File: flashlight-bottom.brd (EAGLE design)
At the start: 33 x 33 mm, 1 part, among them SW1 DIL3-TOGGLE-SWITCHDIL3

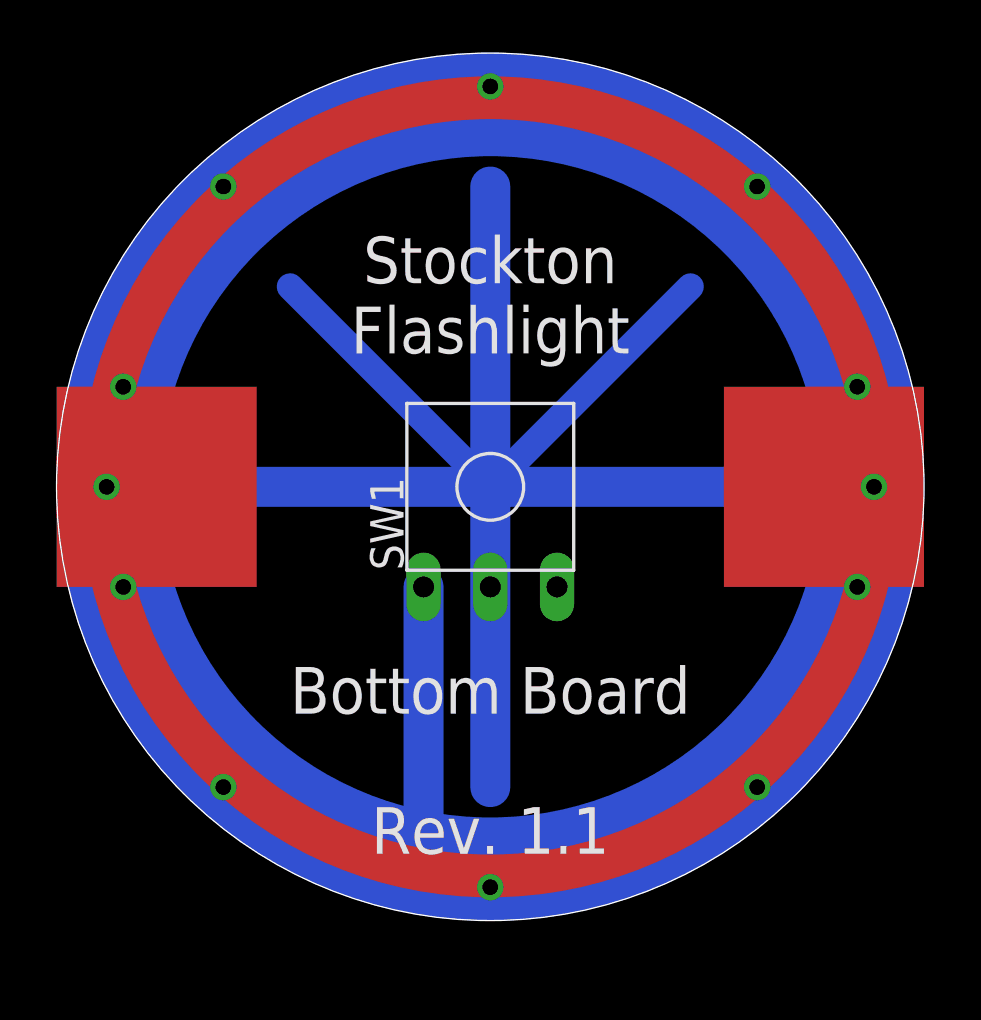
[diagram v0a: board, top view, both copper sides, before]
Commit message: rev 2.0 of the bottom board, plus minor tweaks to the top board
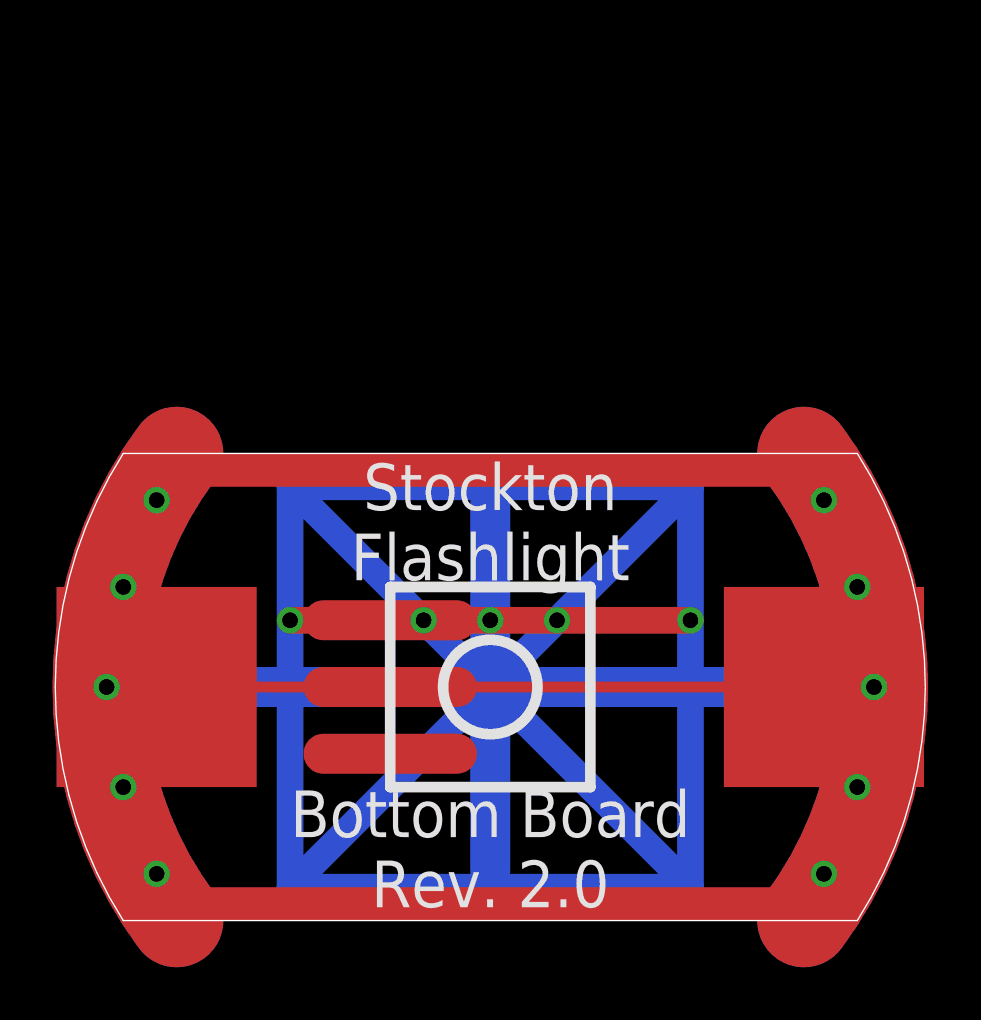
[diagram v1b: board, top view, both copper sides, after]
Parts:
- removed SW1: DIL3-TOGGLE-SWITCHDIL3, chrisy-components:DIL3-TOGGLE-SWITCH
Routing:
- net N$2: track 44.4 -> 156.1 mm, vias 0 -> 5
- net N$16: track 0.00 -> 35.6 mm
- net N$10: track 0.00 -> 33.0 mm, vias 1 -> 0
- net N$5: track 8.89 -> 35.6 mm
- net N$3: track 22.9 -> 0.00 mm
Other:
- board size 33 x 33 mm -> 33.1 x 17.8 mm
- board text added: "Bottom Board Rev. 2.0"
- board text removed: "Bottom Board Rev. 1.1"
- board text removed: "Rev. 1.1"
- board text removed: "SPRING"
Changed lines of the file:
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@@
 <board>
 <plain>
-<circle x="16.51" y="16.51" radius="16.51" width="0.040640625" layer="20"/>
-<circle x="16.51" y="16.51" radius="14.5542" width="3.937" layer="16"/>
-<text x="16.51" y="21.59" size="1.778" layer="25" align="bottom-center">Stockton
+<text x="16.51" y="12.954" size="1.778" layer="25" align="bottom-center">Stockton
 Flashlight</text>
-<circle x="16.51" y="16.51" radius="14.7574" width="3.556" layer="30"/>
-<text x="16.51" y="2.54" size="1.778" layer="1" align="bottom-center">Rev. 1.1</text>
-<text x="16.51" y="2.54" size="1.778" layer="25" align="bottom-center">Bottom Board
-Rev. 1.1</text>
-<circle x="16.51" y="16.51" radius="14.810615625" width="1.6256" layer="1"/>
-<wire x1="16.51" y1="16.51" x2="8.89" y2="24.13" width="1.016" layer="30"/>
-<wire x1="16.51" y1="16.51" x2="5.08" y2="16.51" width="1.524" layer="30"/>
-<wire x1="16.51" y1="16.51" x2="27.94" y2="16.51" width="1.524" layer="30"/>
-<wire x1="16.51" y1="16.51" x2="24.13" y2="24.13" width="1.016" layer="30"/>
-<wire x1="16.51" y1="16.51" x2="16.51" y2="27.94" width="1.524" layer="30"/>
-<wire x1="16.51" y1="16.51" x2="16.51" y2="15.24" width="1.524" layer="30"/>
-<wire x1="16.51" y1="10.16" x2="16.51" y2="5.08" width="1.524" layer="30"/>
-<circle x="16.51" y="16.51" radius="6.35" width="0.4064" layer="22"/>
-<text x="22.352" y="14.605" size="1.016" layer="26" rot="MR0">SPRING</text>
-<rectangle x1="25.4" y1="12.7" x2="33.02" y2="20.32" layer="1"/>
-<rectangle x1="25.4" y1="12.7" x2="33.02" y2="20.32" layer="29"/>
-<rectangle x1="0" y1="12.7" x2="7.62" y2="20.32" layer="29"/>
-<rectangle x1="0" y1="12.7" x2="7.62" y2="20.32" layer="1"/>
+<text x="16.51" y="0.508" size="1.778" layer="25" align="bottom-center">Bottom Board
+Rev. 2.0</text>
+<wire x1="16.51" y1="8.89" x2="8.89" y2="16.51" width="1.016" layer="30"/>
+<wire x1="16.51" y1="8.89" x2="5.08" y2="8.89" width="1.524" layer="30"/>
+<wire x1="16.51" y1="8.89" x2="27.94" y2="8.89" width="1.524" layer="30"/>
+<wire x1="16.51" y1="8.89" x2="24.13" y2="16.51" width="1.016" layer="30"/>
+<wire x1="16.51" y1="8.89" x2="16.51" y2="15.875" width="1.524" layer="30"/>
+<wire x1="16.51" y1="8.89" x2="16.51" y2="1.905" width="1.524" layer="30"/>
+<circle x="16.51" y="8.89" radius="6.35" width="0.4064" layer="22"/>
+<rectangle x1="25.4" y1="5.08" x2="33.02" y2="12.7" layer="1"/>
+<rectangle x1="25.4" y1="5.08" x2="33.02" y2="12.7" layer="29"/>
+<rectangle x1="0" y1="5.08" x2="7.62" y2="12.7" layer="29"/>
+<rectangle x1="0" y1="5.08" x2="7.62" y2="12.7" layer="1"/>
+<wire x1="2.54" y1="17.78" x2="2.54" y2="0" width="0.0508" layer="20" curve="64.94"/>
+<wire x1="30.48" y1="0" x2="30.48" y2="17.78" width="0.0508" layer="20" curve="64.94"/>
+<wire x1="2.54" y1="0" x2="30.48" y2="0" width="0.0508" layer="20"/>
+<wire x1="30.48" y1="17.78" x2="2.54" y2="17.78" width="0.0508" layer="20"/>
+<wire x1="4.572" y1="17.78" x2="4.572" y2="0" width="3.556" layer="30" curve="73.34" cap="flat"/>
+<wire x1="28.448" y1="0" x2="28.448" y2="17.78" width="3.556" layer="30" curve="73.34" cap="flat"/>
+<rectangle x1="2.54" y1="0" x2="30.48" y2="1.27" layer="1"/>
+<rectangle x1="2.54" y1="16.51" x2="30.48" y2="17.78" layer="1"/>
+<wire x1="16.51" y1="8.89" x2="8.89" y2="1.27" width="1.016" layer="30"/>
+<wire x1="16.51" y1="8.89" x2="24.13" y2="1.27" width="1.016" layer="30"/>
+<wire x1="10.16" y1="8.89" x2="15.24" y2="8.89" width="1.524" layer="29"/>
+<wire x1="10.16" y1="11.43" x2="15.24" y2="11.43" width="1.524" layer="29"/>
+<wire x1="10.16" y1="6.35" x2="15.24" y2="6.35" width="1.524" layer="29"/>
+<wire x1="12.7" y1="12.7" x2="20.32" y2="12.7" width="0.4064" layer="25"/>
+<wire x1="20.32" y1="12.7" x2="20.32" y2="5.08" width="0.4064" layer="25"/>
+<wire x1="20.32" y1="5.08" x2="12.7" y2="5.08" width="0.4064" layer="25"/>
+<wire x1="12.7" y1="5.08" x2="12.7" y2="12.7" width="0.4064" layer="25"/>
+<circle x="16.51" y="8.89" radius="1.79605" width="0.4064" layer="25"/>
 </plain>
 <attributes>
@@
 </autorouter>
 <elements>
-<element name="SW1" library="chrisy-components" package="DIL3-TOGGLE-SWITCH" value="DIL3-TOGGLE-SWITCHDIL3" x="16.51" y="16.51"/>
 </elements>
 <signals>
 <signal name="N$1">
-<via x="1.905" y="16.51" extent="1-16" drill="0.6"/>
+<via x="1.905" y="8.89" extent="1-16" drill="0.6"/>
 </signal>
 <signal name="N$4">
-<via x="31.115" y="16.51" extent="1-16" drill="0.6"/>
+<via x="31.115" y="8.89" extent="1-16" drill="0.6"/>
 </signal>
 <signal name="N$2">
-<wire x1="5.08" y1="16.51" x2="16.51" y2="16.51" width="1.524" layer="16"/>
-<wire x1="16.51" y1="16.51" x2="27.94" y2="16.51" width="1.524" layer="16"/>
-<wire x1="16.51" y1="16.51" x2="8.89" y2="24.13" width="1.016" layer="16"/>
-<wire x1="16.51" y1="16.51" x2="24.13" y2="24.13" width="1.016" layer="16"/>
-</signal>
-<signal name="N$3">
-<wire x1="16.51" y1="27.94" x2="16.51" y2="5.08" width="1.524" layer="16"/>
+<wire x1="5.08" y1="8.89" x2="16.51" y2="8.89" width="1.524" layer="16"/>
+<wire x1="16.51" y1="8.89" x2="27.94" y2="8.89" width="1.524" layer="16"/>
+<wire x1="16.51" y1="8.89" x2="13.97" y2="11.43" width="1.016" layer="16"/>
+<wire x1="13.97" y1="11.43" x2="8.89" y2="16.51" width="1.016" layer="16"/>
+<wire x1="16.51" y1="8.89" x2="19.05" y2="11.43" width="1.016" layer="16"/>
+<wire x1="19.05" y1="11.43" x2="24.13" y2="16.51" width="1.016" layer="16"/>
+<wire x1="16.51" y1="8.89" x2="8.89" y2="1.27" width="1.016" layer="16"/>
+<wire x1="16.51" y1="8.89" x2="24.13" y2="1.27" width="1.016" layer="16"/>
+<wire x1="24.13" y1="1.27" x2="8.89" y2="1.27" width="1.016" layer="16"/>
+<wire x1="8.89" y1="1.27" x2="8.89" y2="11.43" width="1.016" layer="16"/>
+<wire x1="8.89" y1="11.43" x2="8.89" y2="16.51" width="1.016" layer="16"/>
+<wire x1="8.89" y1="16.51" x2="24.13" y2="16.51" width="1.016" layer="16"/>
+<wire x1="24.13" y1="16.51" x2="24.13" y2="11.43" width="1.016" layer="16"/>
+<wire x1="24.13" y1="11.43" x2="24.13" y2="1.27" width="1.016" layer="16"/>
+<wire x1="8.89" y1="11.43" x2="13.97" y2="11.43" width="1.016" layer="1"/>
+<via x="8.89" y="11.43" extent="1-16" drill="0.6"/>
+<wire x1="13.97" y1="11.43" x2="16.51" y2="11.43" width="1.016" layer="1"/>
+<wire x1="16.51" y1="11.43" x2="19.05" y2="11.43" width="1.016" layer="1"/>
+<wire x1="19.05" y1="11.43" x2="24.13" y2="11.43" width="1.016" layer="1"/>
+<wire x1="16.51" y1="15.875" x2="16.51" y2="11.43" width="1.524" layer="16"/>
+<wire x1="16.51" y1="11.43" x2="16.51" y2="1.905" width="1.524" layer="16"/>
+<via x="16.51" y="11.43" extent="1-16" drill="0.6"/>
+<via x="24.13" y="11.43" extent="1-16" drill="0.6"/>
+<via x="19.05" y="11.43" extent="1-16" drill="0.6"/>
+<via x="13.97" y="11.43" extent="1-16" drill="0.6"/>
+</signal>
+<signal name="N$12">
+<via x="2.54" y="12.7" extent="1-16" drill="0.6"/>
+</signal>
+<signal name="N$13">
+<via x="2.54" y="5.08" extent="1-16" drill="0.6"/>
+</signal>
+<signal name="N$14">
+<via x="30.48" y="5.08" extent="1-16" drill="0.6"/>
+</signal>
+<signal name="N$15">
+<via x="30.48" y="12.7" extent="1-16" drill="0.6"/>
+</signal>
+<signal name="N$16">
+<wire x1="4.572" y1="17.78" x2="4.572" y2="0" width="3.556" layer="16" curve="73.34" cap="flat"/>
+<wire x1="28.448" y1="0" x2="28.448" y2="17.78" width="3.556" layer="16" curve="73.34" cap="flat"/>
 </signal>
 <signal name="N$5">
-<wire x1="13.97" y1="3.81" x2="13.97" y2="12.7" width="1.524" layer="16"/>
+<wire x1="4.572" y1="17.78" x2="4.572" y2="0" width="3.556" layer="1" curve="73.34" cap="flat"/>
+<wire x1="28.448" y1="0" x2="28.448" y2="17.78" width="3.556" layer="1" curve="73.34" cap="flat"/>
 </signal>
 <signal name="N$6">
-<via x="16.51" y="1.27" extent="1-16" drill="0.6"/>
+<via x="3.81" y="1.778" extent="1-16" drill="0.6"/>
 </signal>
 <signal name="N$7">
-<via x="16.51" y="31.75" extent="1-16" drill="0.6"/>
+<via x="3.81" y="16.002" extent="1-16" drill="0.6"/>
 </signal>
 <signal name="N$8">
-<via x="6.35" y="27.94" extent="1-16" drill="0.6"/>
+<via x="29.21" y="1.778" extent="1-16" drill="0.6"/>
 </signal>
 <signal name="N$9">
-<via x="26.67" y="27.94" extent="1-16" drill="0.6"/>
+<via x="29.21" y="16.002" extent="1-16" drill="0.6"/>
 </signal>
 <signal name="N$10">
-<via x="26.67" y="5.08" extent="1-16" drill="0.6"/>
-</signal>
-<signal name="N$11">
-<via x="6.35" y="5.08" extent="1-16" drill="0.6"/>
-</signal>
-<signal name="N$12">
-<via x="2.54" y="20.32" extent="1-16" drill="0.6"/>
-</signal>
-<signal name="N$13">
-<via x="2.54" y="12.7" extent="1-16" drill="0.6"/>
-</signal>
-<signal name="N$14">
-<via x="30.48" y="12.7" extent="1-16" drill="0.6"/>
-</signal>
-<signal name="N$15">
-<via x="30.48" y="20.32" extent="1-16" drill="0.6"/>
+<wire x1="5.08" y1="8.89" x2="10.16" y2="8.89" width="0.4064" layer="1"/>
+<wire x1="15.24" y1="8.89" x2="27.94" y2="8.89" width="0.4064" layer="1"/>
+<wire x1="10.16" y1="8.89" x2="15.24" y2="8.89" width="1.524" layer="1"/>
+<wire x1="10.16" y1="6.35" x2="15.24" y2="6.35" width="1.524" layer="1"/>
+<wire x1="10.16" y1="11.43" x2="15.24" y2="11.43" width="1.524" layer="1"/>
 </signal>
 </signals>

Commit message: rev 3 of the bottom
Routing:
- net N$10: track 33.0 -> 35.6 mm
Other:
- board text added: "3x C battery This end (-)"
- board text added: "Bottom Board Rev. 3.0"
- board text added: "SPRING"
- board text added: "SW1"
- board text removed: "Bottom Board Rev. 2.0"
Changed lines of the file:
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@@
 <board>
 <plain>
-<text x="16.51" y="12.954" size="1.778" layer="25" align="bottom-center">Stockton
+<text x="16.51" y="13.208" size="1.778" layer="29" align="bottom-center">Stockton
 Flashlight</text>
-<text x="16.51" y="0.508" size="1.778" layer="25" align="bottom-center">Bottom Board
-Rev. 2.0</text>
+<text x="16.51" y="0.508" size="1.778" layer="29" align="bottom-center">Bottom Board
+Rev. 3.0</text>
 <wire x1="16.51" y1="8.89" x2="8.89" y2="16.51" width="1.016" layer="30"/>
 <wire x1="16.51" y1="8.89" x2="5.08" y2="8.89" width="1.524" layer="30"/>
@@
 <wire x1="16.51" y1="8.89" x2="16.51" y2="15.875" width="1.524" layer="30"/>
 <wire x1="16.51" y1="8.89" x2="16.51" y2="1.905" width="1.524" layer="30"/>
-<circle x="16.51" y="8.89" radius="6.35" width="0.4064" layer="22"/>
+<circle x="16.51" y="8.89" radius="6.35" width="0.254" layer="22"/>
 <rectangle x1="25.4" y1="5.08" x2="33.02" y2="12.7" layer="1"/>
 <rectangle x1="25.4" y1="5.08" x2="33.02" y2="12.7" layer="29"/>
@@
 <wire x1="16.51" y1="8.89" x2="8.89" y2="1.27" width="1.016" layer="30"/>
 <wire x1="16.51" y1="8.89" x2="24.13" y2="1.27" width="1.016" layer="30"/>
-<wire x1="10.16" y1="8.89" x2="15.24" y2="8.89" width="1.524" layer="29"/>
-<wire x1="10.16" y1="11.43" x2="15.24" y2="11.43" width="1.524" layer="29"/>
-<wire x1="10.16" y1="6.35" x2="15.24" y2="6.35" width="1.524" layer="29"/>
-<wire x1="12.7" y1="12.7" x2="20.32" y2="12.7" width="0.4064" layer="25"/>
-<wire x1="20.32" y1="12.7" x2="20.32" y2="5.08" width="0.4064" layer="25"/>
-<wire x1="20.32" y1="5.08" x2="12.7" y2="5.08" width="0.4064" layer="25"/>
-<wire x1="12.7" y1="5.08" x2="12.7" y2="12.7" width="0.4064" layer="25"/>
-<circle x="16.51" y="8.89" radius="1.79605" width="0.4064" layer="25"/>
+<wire x1="8.89" y1="8.89" x2="15.24" y2="8.89" width="1.524" layer="29"/>
+<wire x1="8.89" y1="11.43" x2="15.24" y2="11.43" width="1.524" layer="29"/>
+<wire x1="8.89" y1="6.35" x2="15.24" y2="6.35" width="1.524" layer="29"/>
+<wire x1="12.7" y1="12.7" x2="20.32" y2="12.7" width="0.254" layer="25"/>
+<wire x1="20.32" y1="12.7" x2="20.32" y2="5.08" width="0.254" layer="25"/>
+<wire x1="20.32" y1="5.08" x2="12.7" y2="5.08" width="0.254" layer="25"/>
+<wire x1="12.7" y1="5.08" x2="12.7" y2="12.7" width="0.254" layer="25"/>
+<circle x="16.51" y="8.89" radius="1.79605" width="0.254" layer="25"/>
+<rectangle x1="7.112" y1="1.27" x2="25.908" y2="5.08" layer="1"/>
+<rectangle x1="7.366" y1="12.7" x2="25.654" y2="16.764" layer="1"/>
+<rectangle x1="7.366" y1="12.446" x2="25.4" y2="12.7" layer="1"/>
+<rectangle x1="7.112" y1="5.08" x2="25.654" y2="5.334" layer="1"/>
+<rectangle x1="3.556" y1="0.762" x2="7.62" y2="5.334" layer="1"/>
+<rectangle x1="25.4" y1="1.016" x2="30.48" y2="5.334" layer="1"/>
+<rectangle x1="25.654" y1="12.7" x2="29.21" y2="16.764" layer="1"/>
+<rectangle x1="3.556" y1="12.446" x2="7.366" y2="16.764" layer="1"/>
+<text x="22.606" y="6.604" size="1.778" layer="25" rot="R90">SW1</text>
+<text x="25.908" y="7.874" size="1.016" layer="26" rot="MR270">SPRING</text>
+<wire x1="25.146" y1="7.874" x2="25.146" y2="17.526" width="0.4064" layer="22"/>
+<wire x1="25.146" y1="17.526" x2="7.874" y2="17.526" width="0.4064" layer="22"/>
+<wire x1="7.874" y1="17.526" x2="7.874" y2="0.254" width="0.4064" layer="22"/>
+<wire x1="7.874" y1="0.254" x2="25.146" y2="0.254" width="0.4064" layer="22"/>
+<wire x1="25.146" y1="0.254" x2="25.146" y2="2.286" width="0.4064" layer="22"/>
+<text x="7.62" y="15.748" size="1.016" layer="22" rot="MR270"> 3x C  battery
+ This  end (-)</text>
 </plain>
 <attributes>
@@
 <classes>
 <class number="0" name="default" width="0" drill="0">
+<clearance class="0" value="0.205"/>
 </class>
 </classes>
@@
 </signal>
 <signal name="N$10">
-<wire x1="5.08" y1="8.89" x2="10.16" y2="8.89" width="0.4064" layer="1"/>
-<wire x1="15.24" y1="8.89" x2="27.94" y2="8.89" width="0.4064" layer="1"/>
-<wire x1="10.16" y1="8.89" x2="15.24" y2="8.89" width="1.524" layer="1"/>
-<wire x1="10.16" y1="6.35" x2="15.24" y2="6.35" width="1.524" layer="1"/>
-<wire x1="10.16" y1="11.43" x2="15.24" y2="11.43" width="1.524" layer="1"/>
+<wire x1="5.08" y1="8.89" x2="8.89" y2="8.89" width="0.8128" layer="1"/>
+<wire x1="15.24" y1="8.89" x2="27.94" y2="8.89" width="0.8128" layer="1"/>
+<wire x1="8.89" y1="8.89" x2="15.24" y2="8.89" width="1.524" layer="1"/>
+<wire x1="8.89" y1="6.35" x2="15.24" y2="6.35" width="1.524" layer="1"/>
+<wire x1="8.89" y1="11.43" x2="15.24" y2="11.43" width="1.524" layer="1"/>
 </signal>
 </signals>
